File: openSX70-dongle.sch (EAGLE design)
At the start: 22 parts, among them J1 AUDIO_JACK_3.5MM_PTH

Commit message: version 1.3
Fixing stuff
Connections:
- removed net GND-ISO: DS2408.P3, R2.2, R3.1, R4.1, R5.1, R5.2, R7.2, SW1.8
- net GND: now also DS2408.P3, R2.2, R3.1, R4.1, R5.1, R5.2, R7.2, R8.2, SW1.8
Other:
- moved on the sheet: J1, OK1, R7, R8, S1, S2

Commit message: version 2.0 dongle
EagleCAD version 2.0 dongle
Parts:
- renumbered J1 to PC-FLASH, OK1 to OPTO, SW1 to SELECTOR, TP-I/O to TP_I/O
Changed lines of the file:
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@@
 <?xml version="1.0" encoding="utf-8"?>
 <!DOCTYPE eagle SYSTEM "eagle.dtd">
-<eagle version="8.4.2">
+<eagle version="8.4.3">
 <drawing>
 <settings>
@@
 <part name="R8" library="rcl" library_urn="urn:adsk.eagle:library:334" deviceset="R-US_" device="M0805" package3d_urn="urn:adsk.eagle:package:23556/1" value="100K"/>
 <part name="R9" library="rcl" library_urn="urn:adsk.eagle:library:334" deviceset="R-US_" device="M0805" package3d_urn="urn:adsk.eagle:package:23556/1" value="220R"/>
-<part name="SW1" library="special" library_urn="urn:adsk.eagle:library:367" deviceset="SW-C16" device="" package3d_urn="urn:adsk.eagle:package:26665/1"/>
+<part name="SELECTOR" library="special" library_urn="urn:adsk.eagle:library:367" deviceset="SW-C16" device="" package3d_urn="urn:adsk.eagle:package:26665/1"/>
 <part name="SUPPLY4" library="SparkFun-PowerSymbols" library_urn="urn:adsk.eagle:library:530" deviceset="VCC" device=""/>
 <part name="GND-ISO1" library="supply2" library_urn="urn:adsk.eagle:library:372" deviceset="GND" device=""/>
@@
 <part name="LED1" library="adafruit" library_urn="urn:adsk.eagle:library:420" deviceset="LED" device="3MM"/>
 <part name="SUPPLY7" library="SparkFun-PowerSymbols" library_urn="urn:adsk.eagle:library:530" deviceset="VCC" device=""/>
-<part name="OK1" library="openSX70" deviceset="TLP127" device="" value="TLP127"/>
+<part name="OPTO" library="openSX70" deviceset="TLP127" device="" value="TLP127"/>
 <part name="R12" library="rcl" library_urn="urn:adsk.eagle:library:334" deviceset="R-US_" device="M0805" package3d_urn="urn:adsk.eagle:package:23556/1" value="220R"/>
 <part name="GND-ISO10" library="supply2" library_urn="urn:adsk.eagle:library:372" deviceset="GND" device=""/>
 <part name="R13" library="rcl" library_urn="urn:adsk.eagle:library:334" deviceset="R-US_" device="M0805" package3d_urn="urn:adsk.eagle:package:23556/1" value="100K"/>
 <part name="SUPPLY8" library="SparkFun-PowerSymbols" library_urn="urn:adsk.eagle:library:530" deviceset="VCC" device=""/>
-<part name="J1" library="SparkFun-Connectors" deviceset="AUDIO_JACK_3.5MM" device="_PTH"/>
+<part name="PC-FLASH" library="SparkFun-Connectors" deviceset="AUDIO_JACK_3.5MM" device="_PTH"/>
 <part name="FRAME1" library="frames" library_urn="urn:adsk.eagle:library:229" deviceset="DINA4_L" device=""/>
 <part name="GND-ISO3" library="supply2" library_urn="urn:adsk.eagle:library:372" deviceset="GND" device=""/>
 <part name="TP+" library="wirepad" library_urn="urn:adsk.eagle:library:412" deviceset="SMD2" device="" package3d_urn="urn:adsk.eagle:package:30839/1"/>
 <part name="TP-" library="wirepad" library_urn="urn:adsk.eagle:library:412" deviceset="SMD2" device="" package3d_urn="urn:adsk.eagle:package:30839/1"/>
-<part name="TP-I/O" library="wirepad" library_urn="urn:adsk.eagle:library:412" deviceset="SMD2" device="" package3d_urn="urn:adsk.eagle:package:30839/1"/>
+<part name="TP_I/O" library="wirepad" library_urn="urn:adsk.eagle:library:412" deviceset="SMD2" device="" package3d_urn="urn:adsk.eagle:package:30839/1"/>
 <part name="GND-ISO4" library="supply2" library_urn="urn:adsk.eagle:library:372" deviceset="GND" device=""/>
 <part name="GND-ISO6" library="supply2" library_urn="urn:adsk.eagle:library:372" deviceset="GND" device=""/>
@@
 <instance part="R8" gate="G$1" x="172.72" y="63.5" rot="R270"/>
 <instance part="R9" gate="G$1" x="101.6" y="35.56" rot="R180"/>
-<instance part="SW1" gate="G$1" x="134.62" y="137.16" rot="R270"/>
+<instance part="SELECTOR" gate="G$1" x="134.62" y="137.16" rot="R270"/>
 <instance part="SUPPLY4" gate="G$1" x="134.62" y="144.78"/>
 <instance part="GND-ISO1" gate="GND" x="109.22" y="71.12"/>
@@
 <instance part="LED1" gate="G$1" x="91.44" y="35.56" rot="MR270"/>
 <instance part="SUPPLY7" gate="G$1" x="96.52" y="48.26" rot="R270"/>
-<instance part="OK1" gate="G$1" x="78.74" y="50.8" rot="R180"/>
+<instance part="OPTO" gate="G$1" x="78.74" y="50.8" rot="R180"/>
 <instance part="R12" gate="G$1" x="93.98" y="53.34" rot="R180"/>
 <instance part="GND-ISO10" gate="GND" x="109.22" y="48.26"/>
 <instance part="R13" gate="G$1" x="119.38" y="35.56"/>
 <instance part="SUPPLY8" gate="G$1" x="86.36" y="35.56" rot="R90"/>
-<instance part="J1" gate="G$1" x="48.26" y="50.8"/>
+<instance part="PC-FLASH" gate="G$1" x="48.26" y="50.8"/>
 <instance part="FRAME1" gate="G$1" x="-7.62" y="-15.24"/>
 <instance part="FRAME1" gate="G$2" x="154.94" y="-15.24"/>
@@
 <instance part="TP+" gate="1" x="99.06" y="99.06" rot="R270"/>
 <instance part="TP-" gate="1" x="76.2" y="127" rot="R270"/>
-<instance part="TP-I/O" gate="1" x="99.06" y="88.9" rot="R270"/>
+<instance part="TP_I/O" gate="1" x="99.06" y="88.9" rot="R270"/>
 <instance part="GND-ISO4" gate="GND" x="76.2" y="116.84"/>
 <instance part="GND-ISO6" gate="GND" x="193.04" y="38.1" rot="R90"/>
@@
 <segment>
 <pinref part="SUPPLY4" gate="G$1" pin="VCC"/>
-<pinref part="SW1" gate="G$1" pin="C"/>
+<pinref part="SELECTOR" gate="G$1" pin="C"/>
 <wire x1="134.62" y1="144.78" x2="134.62" y2="142.24" width="0.1524" layer="91"/>
 </segment>
@@
 </segment>
 <segment>
-<pinref part="OK1" gate="G$1" pin="A"/>
+<pinref part="OPTO" gate="G$1" pin="A"/>
 <pinref part="SUPPLY7" gate="G$1" pin="VCC"/>
 <wire x1="88.9" y1="48.26" x2="96.52" y2="48.26" width="0.1524" layer="91"/>
@@
 <wire x1="88.9" y1="71.12" x2="88.9" y2="68.58" width="0.1524" layer="91"/>
 <junction x="88.9" y="68.58"/>
-<pinref part="TP-I/O" gate="1" pin="P"/>
+<pinref part="TP_I/O" gate="1" pin="P"/>
 <wire x1="99.06" y1="86.36" x2="99.06" y2="83.82" width="0.1524" layer="91"/>
 <junction x="99.06" y="83.82"/>
@@
 <wire x1="111.76" y1="116.84" x2="111.76" y2="121.92" width="0.1524" layer="91"/>
 <wire x1="111.76" y1="121.92" x2="129.54" y2="121.92" width="0.1524" layer="91"/>
-<pinref part="SW1" gate="G$1" pin="1"/>
+<pinref part="SELECTOR" gate="G$1" pin="1"/>
 <wire x1="129.54" y1="121.92" x2="129.54" y2="132.08" width="0.1524" layer="91"/>
 <pinref part="R2" gate="G$1" pin="1"/>
@@
 <net name="N$4" class="0">
 <segment>
-<pinref part="SW1" gate="G$1" pin="2"/>
+<pinref part="SELECTOR" gate="G$1" pin="2"/>
 <wire x1="134.62" y1="132.08" x2="134.62" y2="121.92" width="0.1524" layer="91"/>
 <wire x1="134.62" y1="121.92" x2="157.48" y2="121.92" width="0.1524" layer="91"/>
@@
 <net name="N$5" class="0">
 <segment>
-<pinref part="SW1" gate="G$1" pin="4"/>
+<pinref part="SELECTOR" gate="G$1" pin="4"/>
 <wire x1="139.7" y1="132.08" x2="139.7" y2="124.46" width="0.1524" layer="91"/>
 <wire x1="139.7" y1="124.46" x2="162.56" y2="124.46" width="0.1524" layer="91"/>
@@
 <net name="N$10" class="0">
 <segment>
-<pinref part="OK1" gate="G$1" pin="C"/>
+<pinref part="OPTO" gate="G$1" pin="C"/>
 <pinref part="R12" gate="G$1" pin="2"/>
 </segment>
@@
 <net name="N$12" class="0">
 <segment>
-<pinref part="J1" gate="G$1" pin="TIP"/>
-<pinref part="OK1" gate="G$1" pin="COL"/>
+<pinref part="PC-FLASH" gate="G$1" pin="TIP"/>
+<pinref part="OPTO" gate="G$1" pin="COL"/>
 <wire x1="53.34" y1="45.72" x2="71.12" y2="45.72" width="0.1524" layer="91"/>
 <wire x1="71.12" y1="45.72" x2="71.12" y2="48.26" width="0.1524" layer="91"/>
@@
 <net name="N$15" class="0">
 <segment>
-<pinref part="OK1" gate="G$1" pin="EMIT"/>
-<pinref part="J1" gate="G$1" pin="RING"/>
+<pinref part="OPTO" gate="G$1" pin="EMIT"/>
+<pinref part="PC-FLASH" gate="G$1" pin="RING"/>
 <wire x1="53.34" y1="53.34" x2="71.12" y2="53.34" width="0.1524" layer="91"/>
 </segment>
@@
 <wire x1="154.94" y1="76.2" x2="167.64" y2="76.2" width="0.1524" layer="91"/>
 <wire x1="167.64" y1="76.2" x2="167.64" y2="93.98" width="0.1524" layer="91"/>
-<pinref part="SW1" gate="G$1" pin="8"/>
+<pinref part="SELECTOR" gate="G$1" pin="8"/>
 <wire x1="167.64" y1="93.98" x2="167.64" y2="114.3" width="0.1524" layer="91"/>
 <wire x1="167.64" y1="114.3" x2="167.64" y2="127" width="0.1524" layer="91"/>
@@
 </sheet>
 </sheets>
+<errors>
+</errors>
 </schematic>
 </drawing>

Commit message: Proper upload of version 2.1 openSX70 dongle
Version 2.1 manufactured by EasyEDA
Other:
- note added: "2.1"
- note removed: "2.0"
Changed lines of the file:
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@@
 <plain>
 <text x="205.74" y="10.16" size="6.4516" layer="91">openSX70</text>
-<text x="244.856" y="-9.398" size="5.08" layer="97">2.0</text>
+<text x="244.856" y="-9.398" size="5.08" layer="97">2.1</text>
 </plain>
 <instances>

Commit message: Moved to 2.2 there was a ground loose on the DS2408!!!
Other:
- note added: "2.2"
- note removed: "2.1"
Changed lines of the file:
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@@
 <plain>
 <text x="205.74" y="10.16" size="6.4516" layer="91">openSX70</text>
-<text x="244.856" y="-9.398" size="5.08" layer="97">2.1</text>
+<text x="244.856" y="-9.398" size="5.08" layer="97">2.2</text>
 </plain>
 <instances>

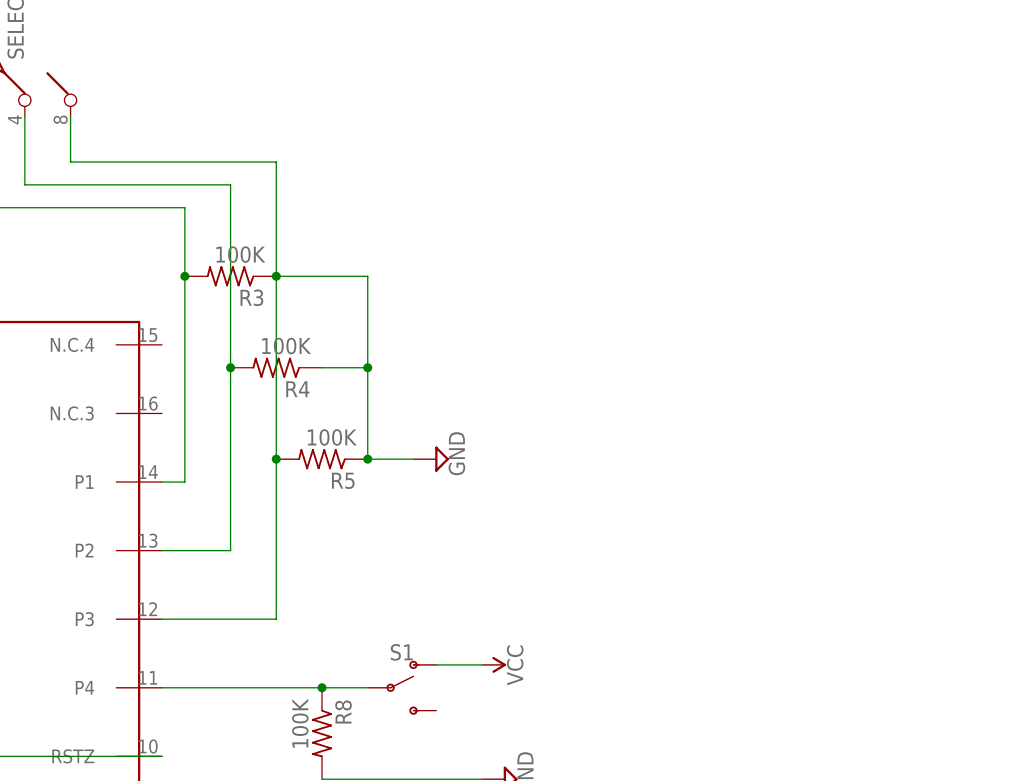
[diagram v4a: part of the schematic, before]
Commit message: Fix big flaws. Selector pin 8 was not connected to P3 (pin 12) D'ho!!
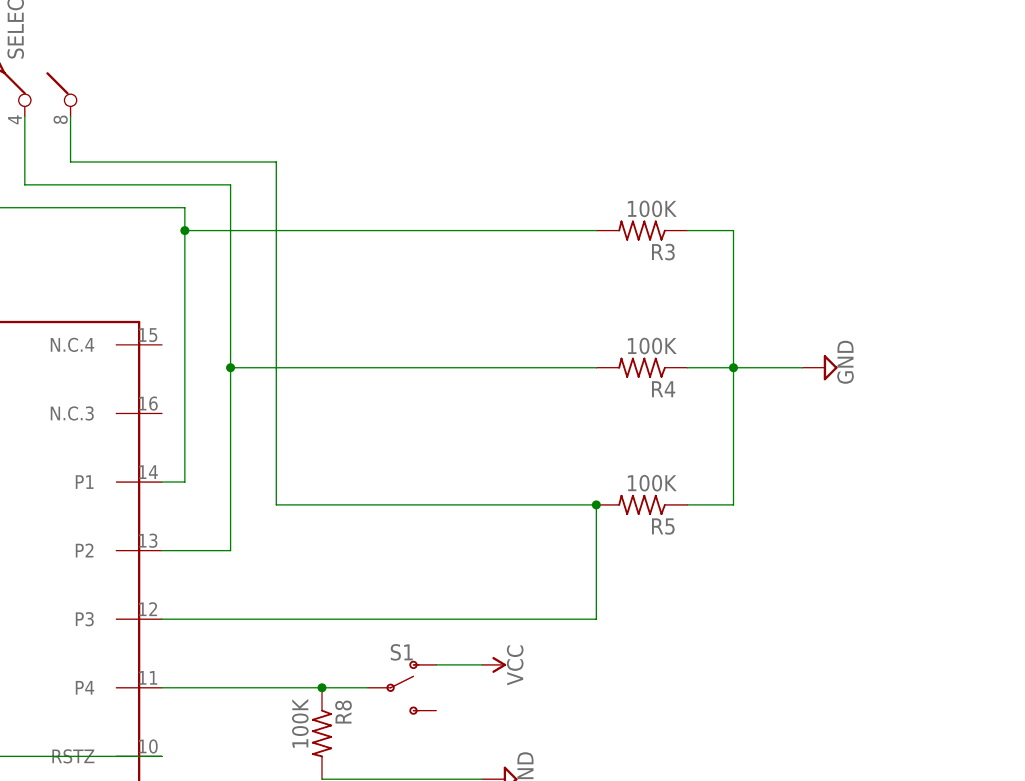
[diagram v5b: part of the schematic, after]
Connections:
- new net N$13: DS2408.P3, R5.2, SELECTOR.8
- net GND: no longer DS2408.P3, R5.2, SELECTOR.8
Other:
- moved on the sheet: R3, R4, R5
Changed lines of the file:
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@@
 <instance part="R1" gate="G$1" x="88.9" y="76.2" rot="R90"/>
 <instance part="R2" gate="G$1" x="106.68" y="116.84" rot="R180"/>
-<instance part="R3" gate="G$1" x="162.56" y="114.3" rot="R180"/>
-<instance part="R4" gate="G$1" x="167.64" y="104.14" rot="R180"/>
-<instance part="R5" gate="G$1" x="172.72" y="93.98" rot="R180"/>
+<instance part="R3" gate="G$1" x="208.28" y="119.38" rot="R180"/>
+<instance part="R4" gate="G$1" x="208.28" y="104.14" rot="R180"/>
+<instance part="R5" gate="G$1" x="208.28" y="88.9" rot="R180"/>
 <instance part="R6" gate="G$1" x="109.22" y="55.88" rot="R270"/>
 <instance part="R7" gate="G$1" x="160.02" y="43.18" rot="R270"/>
@@
 <instance part="GND-ISO6" gate="GND" x="193.04" y="38.1" rot="R90"/>
 <instance part="GND-ISO11" gate="GND" x="96.52" y="116.84" rot="R270"/>
-<instance part="GND-ISO12" gate="GND" x="185.42" y="93.98" rot="R90"/>
+<instance part="GND-ISO12" gate="GND" x="228.6" y="104.14" rot="R90"/>
 </instances>
 <busses>
@@
 <wire x1="134.62" y1="132.08" x2="134.62" y2="121.92" width="0.1524" layer="91"/>
 <wire x1="134.62" y1="121.92" x2="157.48" y2="121.92" width="0.1524" layer="91"/>
-<wire x1="157.48" y1="121.92" x2="157.48" y2="114.3" width="0.1524" layer="91"/>
 <pinref part="DS2408" gate="G$1" pin="P1"/>
-<wire x1="157.48" y1="114.3" x2="157.48" y2="91.44" width="0.1524" layer="91"/>
-<wire x1="157.48" y1="91.44" x2="154.94" y2="91.44" width="0.1524" layer="91"/>
+<wire x1="154.94" y1="91.44" x2="157.48" y2="91.44" width="0.1524" layer="91"/>
+<wire x1="157.48" y1="91.44" x2="157.48" y2="119.38" width="0.1524" layer="91"/>
 <pinref part="R3" gate="G$1" pin="2"/>
-<junction x="157.48" y="114.3"/>
+<wire x1="157.48" y1="119.38" x2="157.48" y2="121.92" width="0.1524" layer="91"/>
+<wire x1="203.2" y1="119.38" x2="157.48" y2="119.38" width="0.1524" layer="91"/>
+<junction x="157.48" y="119.38"/>
 </segment>
 </net>
@@
 <wire x1="139.7" y1="132.08" x2="139.7" y2="124.46" width="0.1524" layer="91"/>
 <wire x1="139.7" y1="124.46" x2="162.56" y2="124.46" width="0.1524" layer="91"/>
-<wire x1="162.56" y1="124.46" x2="162.56" y2="104.14" width="0.1524" layer="91"/>
 <pinref part="DS2408" gate="G$1" pin="P2"/>
-<wire x1="162.56" y1="104.14" x2="162.56" y2="83.82" width="0.1524" layer="91"/>
-<wire x1="162.56" y1="83.82" x2="154.94" y2="83.82" width="0.1524" layer="91"/>
+<wire x1="154.94" y1="83.82" x2="162.56" y2="83.82" width="0.1524" layer="91"/>
+<wire x1="162.56" y1="83.82" x2="162.56" y2="104.14" width="0.1524" layer="91"/>
 <pinref part="R4" gate="G$1" pin="2"/>
+<wire x1="162.56" y1="104.14" x2="162.56" y2="124.46" width="0.1524" layer="91"/>
+<wire x1="203.2" y1="104.14" x2="162.56" y2="104.14" width="0.1524" layer="91"/>
 <junction x="162.56" y="104.14"/>
 </segment>
@@
 </segment>
 <segment>
-<pinref part="R5" gate="G$1" pin="1"/>
-<pinref part="DS2408" gate="G$1" pin="P3"/>
-<wire x1="154.94" y1="76.2" x2="167.64" y2="76.2" width="0.1524" layer="91"/>
-<wire x1="167.64" y1="76.2" x2="167.64" y2="93.98" width="0.1524" layer="91"/>
-<pinref part="SELECTOR" gate="G$1" pin="8"/>
-<wire x1="167.64" y1="93.98" x2="167.64" y2="114.3" width="0.1524" layer="91"/>
-<wire x1="167.64" y1="114.3" x2="167.64" y2="127" width="0.1524" layer="91"/>
-<wire x1="167.64" y1="127" x2="144.78" y2="127" width="0.1524" layer="91"/>
-<wire x1="144.78" y1="127" x2="144.78" y2="132.08" width="0.1524" layer="91"/>
-<pinref part="R3" gate="G$1" pin="1"/>
-<pinref part="R5" gate="G$1" pin="2"/>
-<junction x="167.64" y="93.98"/>
-<wire x1="167.64" y1="114.3" x2="177.8" y2="114.3" width="0.1524" layer="91"/>
-<junction x="167.64" y="114.3"/>
-<pinref part="R4" gate="G$1" pin="1"/>
-<wire x1="177.8" y1="104.14" x2="172.72" y2="104.14" width="0.1524" layer="91"/>
-<wire x1="177.8" y1="114.3" x2="177.8" y2="104.14" width="0.1524" layer="91"/>
-<wire x1="177.8" y1="104.14" x2="177.8" y2="93.98" width="0.1524" layer="91"/>
-<junction x="177.8" y="104.14"/>
-<pinref part="GND-ISO12" gate="GND" pin="GND"/>
-<wire x1="177.8" y1="93.98" x2="182.88" y2="93.98" width="0.1524" layer="91"/>
-<junction x="177.8" y="93.98"/>
-</segment>
-<segment>
 <pinref part="GND-ISO11" gate="GND" pin="GND"/>
 <pinref part="R2" gate="G$1" pin="2"/>
@@
 <pinref part="GND-ISO8" gate="GND" pin="GND"/>
 <wire x1="172.72" y1="58.42" x2="190.5" y2="58.42" width="0.1524" layer="91"/>
+</segment>
+<segment>
+<pinref part="R3" gate="G$1" pin="1"/>
+<wire x1="213.36" y1="119.38" x2="218.44" y2="119.38" width="0.1524" layer="91"/>
+<wire x1="218.44" y1="119.38" x2="218.44" y2="104.14" width="0.1524" layer="91"/>
+<pinref part="R4" gate="G$1" pin="1"/>
+<wire x1="218.44" y1="104.14" x2="213.36" y2="104.14" width="0.1524" layer="91"/>
+<pinref part="GND-ISO12" gate="GND" pin="GND"/>
+<wire x1="218.44" y1="104.14" x2="226.06" y2="104.14" width="0.1524" layer="91"/>
+<junction x="218.44" y="104.14"/>
+<pinref part="R5" gate="G$1" pin="1"/>
+<wire x1="218.44" y1="104.14" x2="218.44" y2="88.9" width="0.1524" layer="91"/>
+<wire x1="218.44" y1="88.9" x2="213.36" y2="88.9" width="0.1524" layer="91"/>
 </segment>
 </net>
@@
 </segment>
 </net>
+<net name="N$13" class="0">
+<segment>
+<pinref part="DS2408" gate="G$1" pin="P3"/>
+<pinref part="R5" gate="G$1" pin="2"/>
+<wire x1="154.94" y1="76.2" x2="203.2" y2="76.2" width="0.1524" layer="91"/>
+<wire x1="203.2" y1="76.2" x2="203.2" y2="88.9" width="0.1524" layer="91"/>
+<wire x1="203.2" y1="88.9" x2="167.64" y2="88.9" width="0.1524" layer="91"/>
+<junction x="203.2" y="88.9"/>
+<pinref part="SELECTOR" gate="G$1" pin="8"/>
+<wire x1="167.64" y1="127" x2="144.78" y2="127" width="0.1524" layer="91"/>
+<wire x1="144.78" y1="127" x2="144.78" y2="132.08" width="0.1524" layer="91"/>
+<wire x1="167.64" y1="88.9" x2="167.64" y2="127" width="0.1524" layer="91"/>
+</segment>
+</net>
